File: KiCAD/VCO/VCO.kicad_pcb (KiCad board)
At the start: 2 copper layers, 215 x 85 mm, 40 parts, among them J1 CV IN 1, J2 CV IN 2, J3 PWM, J4 SAW OUT, J5 PULSE OUT, J6 Conn_01x03_Pin, J7 Conn_01x03_Pin, Q1 NPN, T1 PNP, T2 NPN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

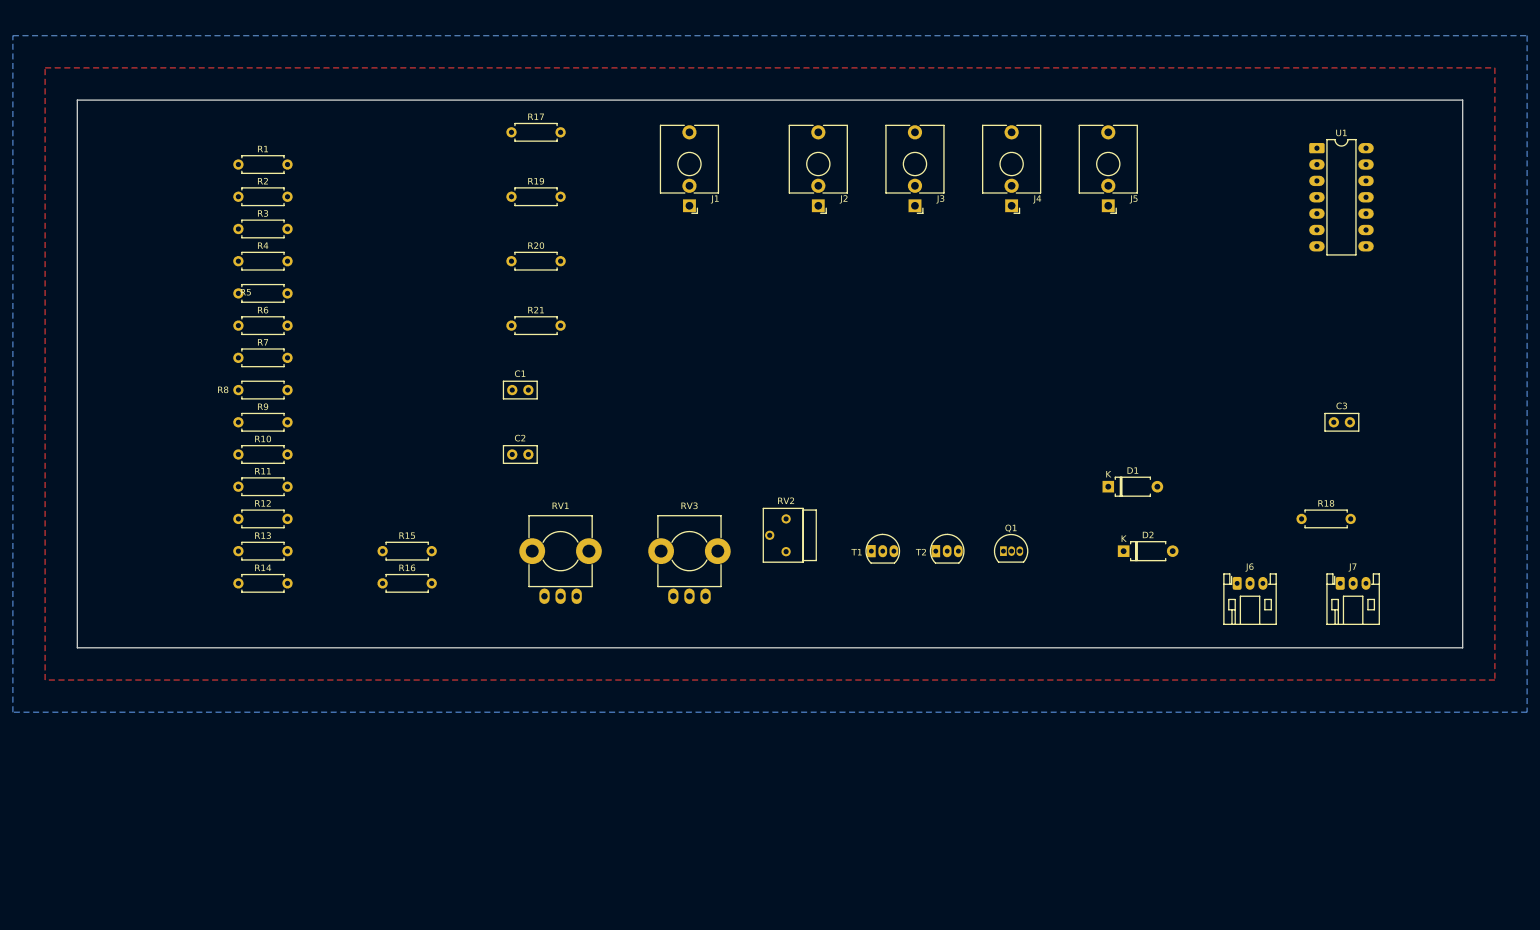
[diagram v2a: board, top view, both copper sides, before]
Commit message: VCO rearrange pcb
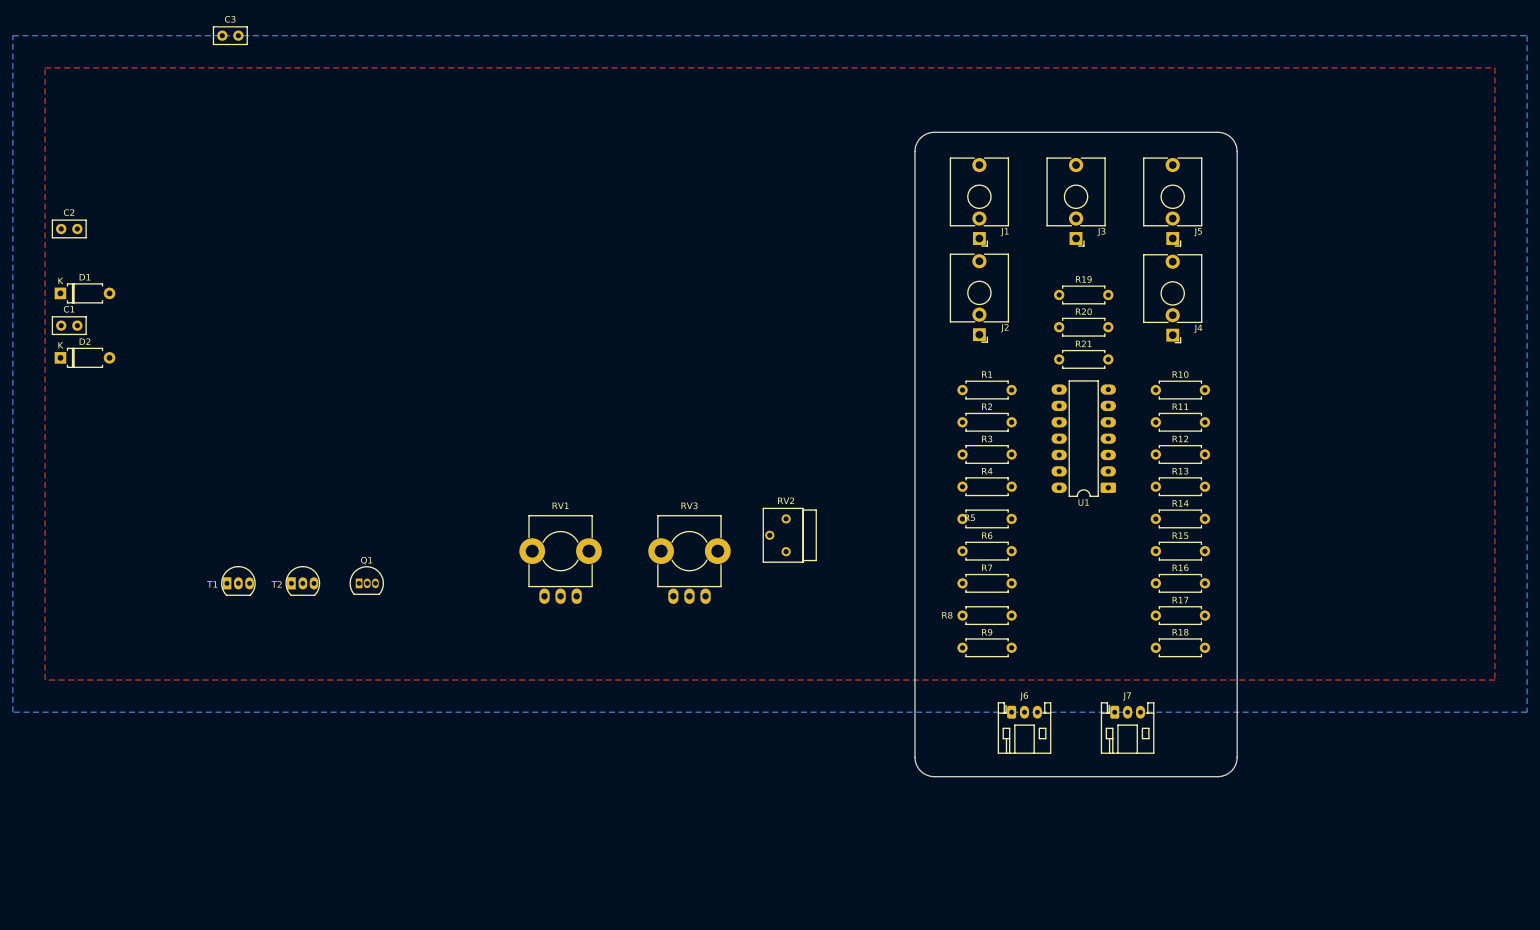
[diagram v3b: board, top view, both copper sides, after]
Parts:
- added REF**: Untitled, HackSynth:Module 50x100mm, F.Cu at (190.0, 95.0)
- moved C3 182.6 mm to (57.5, 30.0)
- moved D2 167.7 mm to (32.4, 80.0)
- moved D1 165.4 mm to (32.4, 70.0)
- moved R10 142.7 mm to (202.4, 85.0)
- moved R11 142.7 mm to (202.4, 90.0)
- moved R12 142.7 mm to (202.4, 95.0)
- moved R13 142.7 mm to (202.4, 100.0)
- moved R14 142.7 mm to (202.4, 105.0)
- moved R17 125.0 mm to (202.4, 120.0)
- moved R15 120.0 mm to (202.4, 110.0)
- moved R16 120.0 mm to (202.4, 115.0)
- moved R1 117.7 mm to (172.4, 85.0)
- moved R2 117.7 mm to (172.4, 90.0)
- moved R3 117.7 mm to (172.4, 95.0)
- moved R4 117.7 mm to (172.4, 100.0)
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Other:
- board size 215 x 85 mm -> 50 x 100 mm

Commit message: VCO pcb board population persists
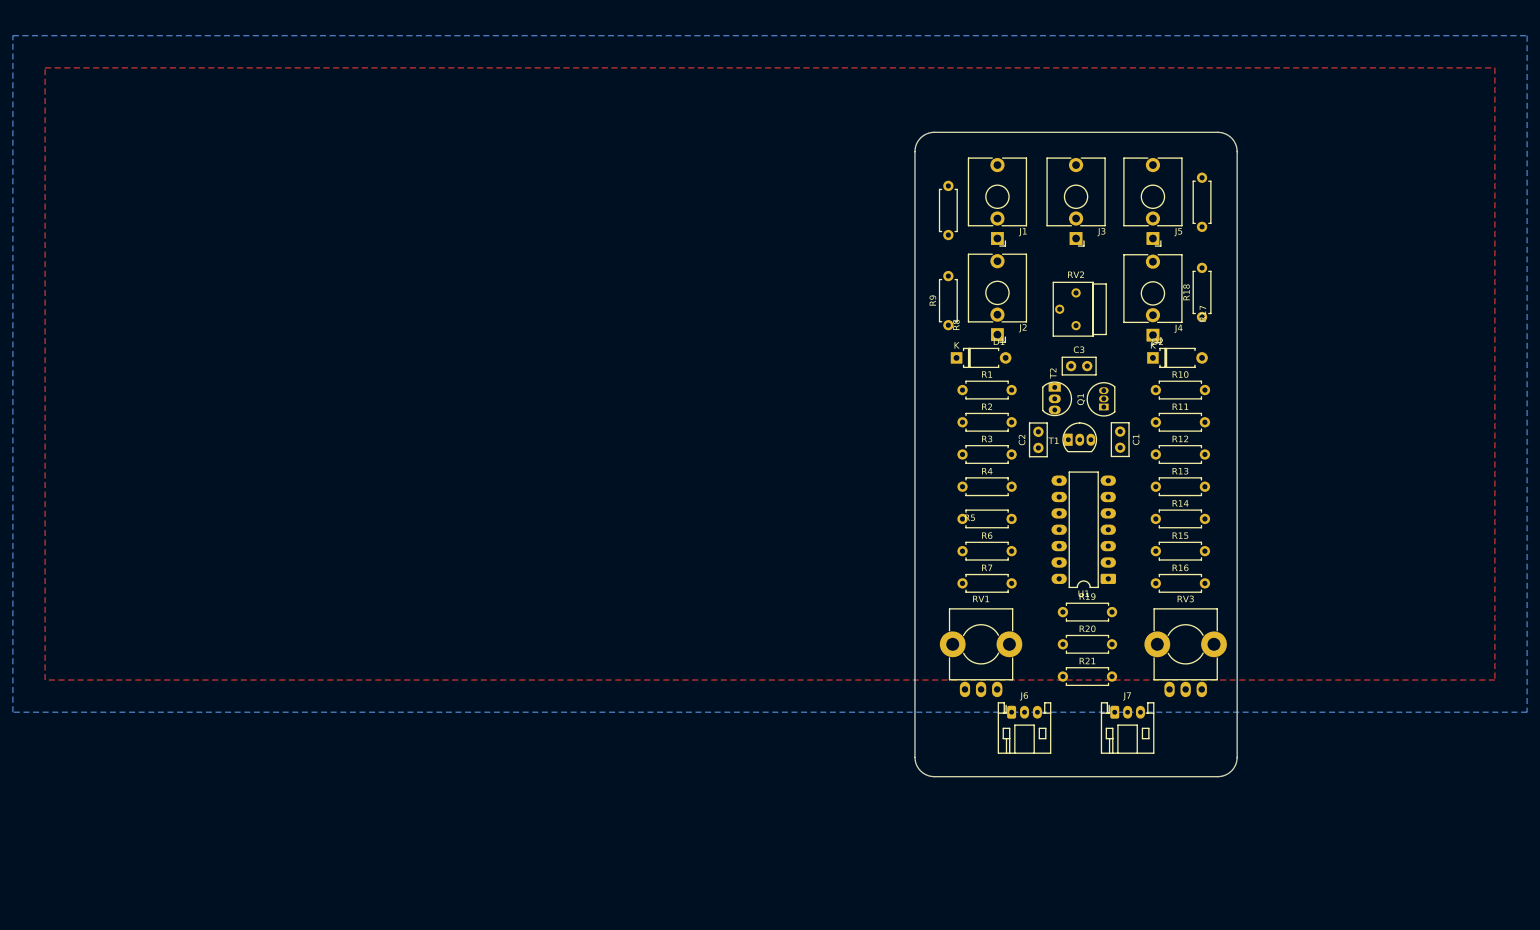
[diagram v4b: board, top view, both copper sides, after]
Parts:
- moved D2 169.6 mm to (201.9, 80.0)
- moved C1 165.2 mm to (196.8, 91.4), turned to -90 degrees
- moved C2 155.4 mm to (184.2, 94.0), turned to 90 degrees
- moved C3 141.4 mm to (189.2, 81.3)
- moved D1 139.4 mm to (171.4, 80.0)
- moved T1 132.5 mm to (189.3, 92.7)
- moved T2 121.7 mm to (186.7, 85.1), turned to -90 degrees
- moved Q1 118.8 mm to (194.3, 87.6), turned to 90 degrees
- moved RV3 78.4 mm to (207.0, 124.5)
- moved RV1 66.8 mm to (175.3, 124.5)
- moved R17 60.8 mm to (209.6, 59.7), turned to 90 degrees
- moved R8 59.1 mm to (170.2, 60.9), turned to 90 degrees
- moved RV2 57.1 mm to (190.0, 69.9)
- moved R18 51.8 mm to (209.6, 73.7), turned to 90 degrees
- moved R9 50.1 mm to (170.2, 74.9), turned to 90 degrees
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
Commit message: Minor VCO update
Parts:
- moved C1 40.3 mm to (156.8, 96.4)
- moved C2 40.3 mm to (144.2, 99.0)
- moved C3 40.3 mm to (149.2, 86.3)
- moved D1 40.3 mm to (131.4, 85.0)
- moved D2 40.3 mm to (161.9, 85.0)
- moved J1 40.3 mm to (137.8, 60.0)
- moved J2 40.3 mm to (137.8, 74.9)
- moved J3 40.3 mm to (150.0, 60.0)
- moved J4 40.3 mm to (161.9, 75.0)
- moved J5 40.3 mm to (161.9, 60.0)
- moved J6 40.3 mm to (140.0, 140.0)
- moved J7 40.3 mm to (156.0, 140.0)
- moved Q1 40.3 mm to (154.3, 92.6)
- moved R1 40.3 mm to (132.4, 90.0)
- moved R10 40.3 mm to (162.4, 90.0)
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
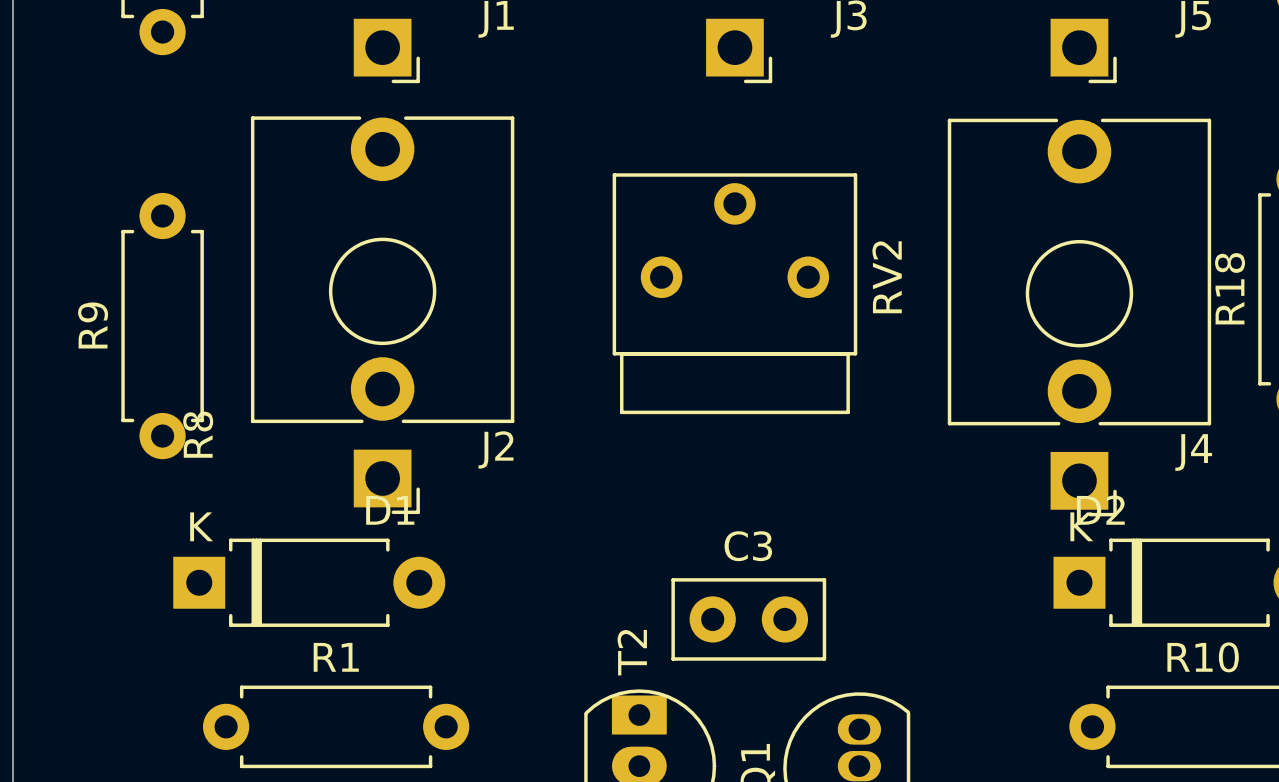
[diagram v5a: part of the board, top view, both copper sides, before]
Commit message: ADSR Rearrange
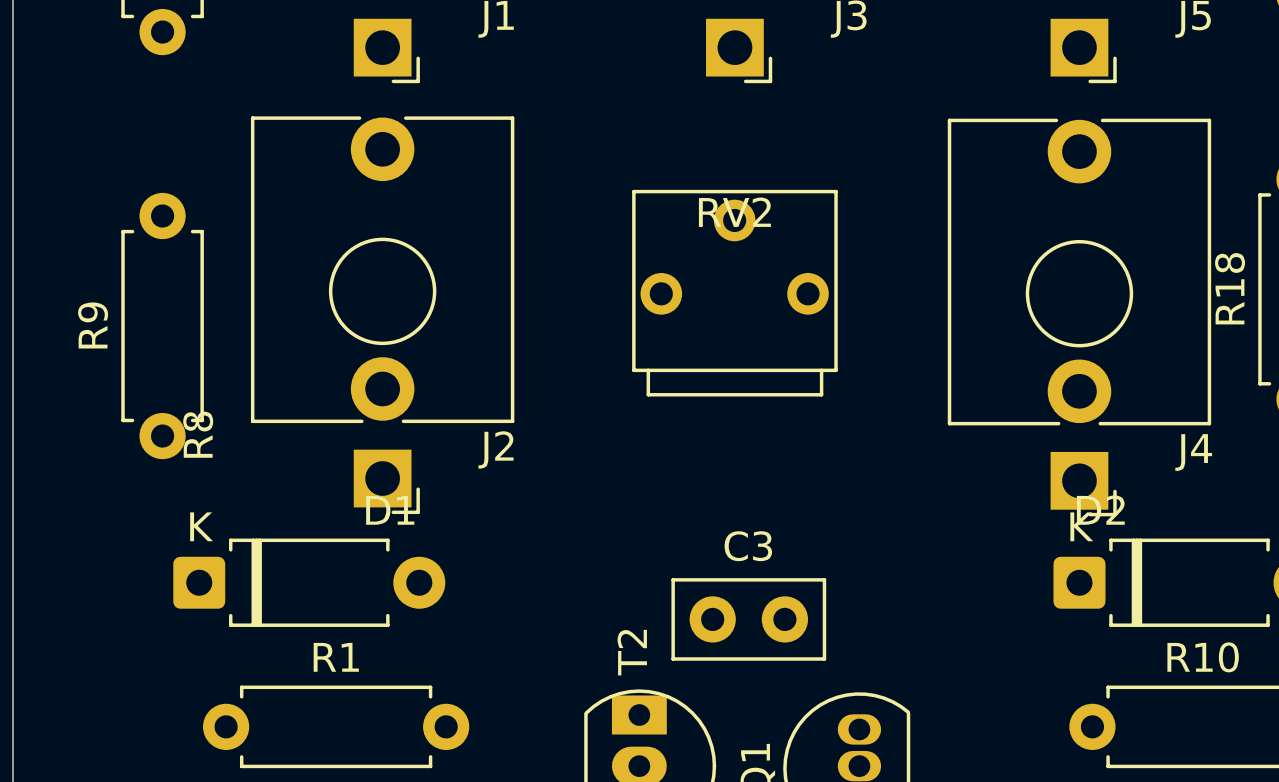
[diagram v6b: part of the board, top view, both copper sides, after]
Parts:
- moved RV2 2.60 mm to (150.0, 75.0), turned to 0 degrees

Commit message: Reapply VCO pcb layout changes.
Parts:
- R4, R5, R6: footprint Resistor_THT:R_Axial_DIN0207_L6.3mm_D2.5mm_P7.62mm_Horizontal -> Resistor_THT:R_Axial_DIN0207_L6.3mm_D2.5mm_P2.54mm_Vertical
- moved R10 112.2 mm to (53.8, 118.2)
- moved R11 111.9 mm to (53.8, 122.0)
- moved R12 111.5 mm to (53.9, 125.8)
- moved D2 97.5 mm to (78.2, 135.1), turned to 90 degrees
- moved C1 88.2 mm to (69.2, 86.5), turned to 180 degrees
- moved R17 85.3 mm to (95.8, 107.5), turned to 180 degrees
- moved U1 85.1 mm to (70.8, 107.6), turned to 0 degrees
- moved R18 82.1 mm to (95.7, 114.5), turned to 180 degrees
- moved R7 80.9 mm to (53.7, 101.2)
- moved R8 80.3 mm to (61.6, 107.8), turned to 180 degrees
- moved J2 79.0 mm to (58.8, 77.5), turned to 90 degrees
- moved J7 79.0 mm to (77.0, 141.8)
- moved D1 78.7 mm to (70.7, 135.0), turned to 90 degrees
- moved R3 78.7 mm to (53.8, 97.5)
- moved R2 78.6 mm to (53.8, 93.8)
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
